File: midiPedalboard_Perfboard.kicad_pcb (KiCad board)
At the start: 8 copper layers, 66 x 50.8 mm, 49 parts, among them J1 wire, J10 wire, J11 wire, J12 wire, J13 wire, J14 wire, J15 MIDI_4, J16 MIDI_5, J17 MIDI_4, J18 MIDI_2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

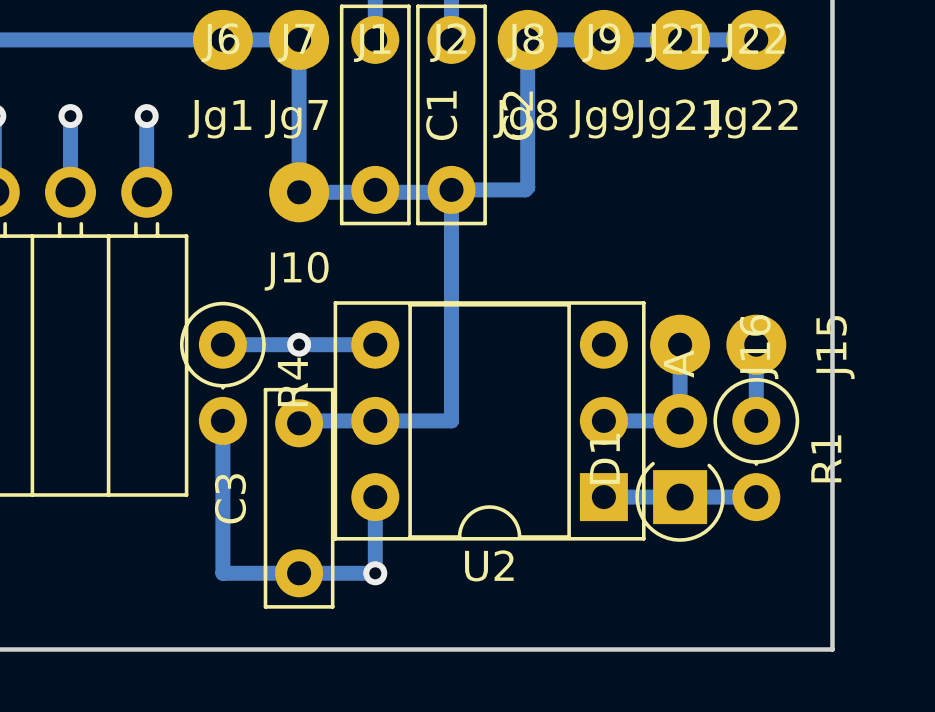
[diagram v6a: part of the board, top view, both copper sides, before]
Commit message: move pc900 part
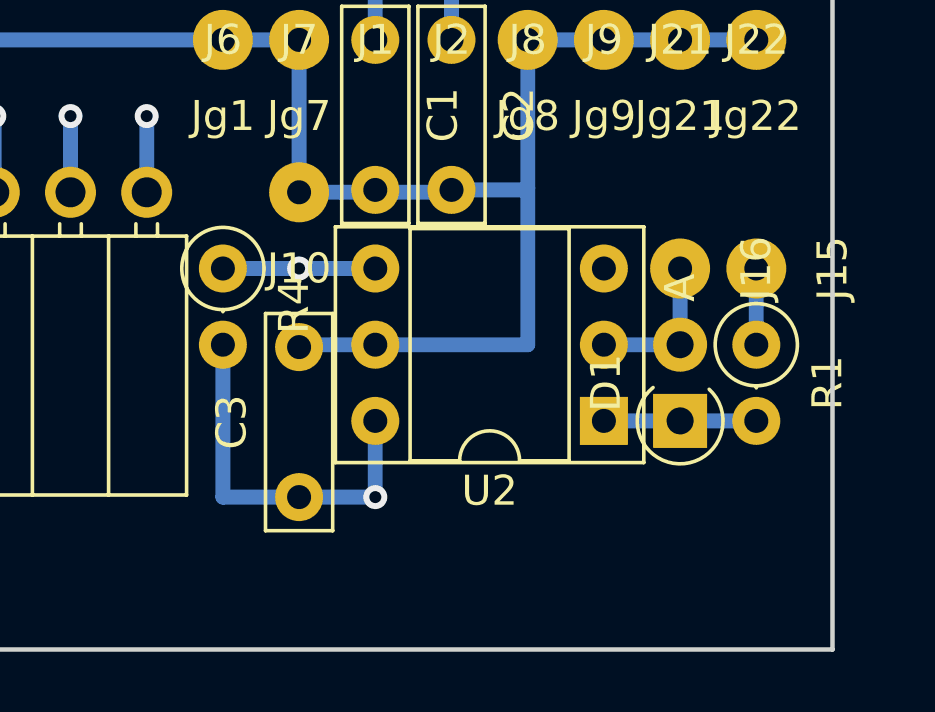
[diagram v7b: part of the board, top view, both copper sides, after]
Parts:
- moved D1 2.54 mm to (172.7, 119.4)
- moved J15 2.54 mm to (175.3, 114.3)
- moved J16 2.54 mm to (172.7, 114.3)
- moved R4 2.54 mm to (157.5, 114.3)
- moved U2 2.54 mm to (170.2, 119.4)
- moved C3 2.54 mm to (160.0, 121.9)
- moved R1 2.54 mm to (175.3, 116.8)
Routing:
- net /UART_RX: track 35.9 -> 33.3 mm
- net VCC: track 129.4 -> 126.9 mm
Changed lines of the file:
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@@
   )
   (module Diode_THT:D_A-405_P2.54mm_Vertical_AnodeUp (layer F.Cu)
-    (at 172.72 121.92 90)
+    (at 172.72 119.38 90)
     (descr "Diode, A-405 series, Axial, Vertical, pin pitch=2.54mm, , length*diameter=5.2*2.7mm^2, , http://www.diodes.com/_files/packages/A-405.pdf")
     (tags "Diode A-405 series Axial Vertical pin pitch 2.54mm  length 5.2mm diameter 2.7mm")
@@
   )
   (module Connector_Wire:SolderWirePad_1x01_Drill0.8mm (layer F.Cu)
-    (at 175.26 116.84 270)
+    (at 175.26 114.3 270)
     (descr "Wire solder connection")
     (tags connector)
@@
   )
   (module Connector_Wire:SolderWirePad_1x01_Drill0.8mm (layer F.Cu)
-    (at 172.72 116.84 270)
+    (at 172.72 114.3 270)
     (descr "Wire solder connection")
     (tags connector)
@@
   )
   (module Resistor_THT:R_Axial_DIN0207_L6.3mm_D2.5mm_P2.54mm_Vertical (layer F.Cu)
-    (at 175.26 119.38 270)
+    (at 175.26 116.84 270)
     (descr "Resistor, Axial_DIN0207 series, Axial, Vertical, pin pitch=2.54mm, 0.25W = 1/4W, length*diameter=6.3*2.5mm^2, http://cdn-reichelt.de/documents/datenblatt/B400/1_4W%23YAG.pdf")
     (tags "Resistor Axial_DIN0207 series Axial Vertical pin pitch 2.54mm 0.25W = 1/4W length 6.3mm diameter 2.5mm")
@@
   )
   (module Resistor_THT:R_Axial_DIN0207_L6.3mm_D2.5mm_P2.54mm_Vertical (layer F.Cu)
-    (at 157.48 116.84 270)
+    (at 157.48 114.3 270)
     (descr "Resistor, Axial_DIN0207 series, Axial, Vertical, pin pitch=2.54mm, 0.25W = 1/4W, length*diameter=6.3*2.5mm^2, http://cdn-reichelt.de/documents/datenblatt/B400/1_4W%23YAG.pdf")
     (tags "Resistor Axial_DIN0207 series Axial Vertical pin pitch 2.54mm 0.25W = 1/4W length 6.3mm diameter 2.5mm")
@@
   )
   (module Package_DIP:DIP-6_W7.62mm_Socket (layer F.Cu)
-    (at 170.18 121.92 180)
+    (at 170.18 119.38 180)
     (descr "6-lead though-hole mounted DIP package, row spacing 7.62 mm (300 mils), Socket")
     (tags "THT DIP DIL PDIP 2.54mm 7.62mm 300mil Socket")
@@
   )
   (module Capacitor_THT:C_Rect_L7.0mm_W2.0mm_P5.00mm (layer F.Cu)
-    (at 160.02 124.46 90)
+    (at 160.02 121.92 90)
     (descr "C, Rect series, Radial, pin pitch=5.00mm, , length*width=7*2mm^2, Capacitor")
     (tags "C Rect series Radial pin pitch 5.00mm  length 7mm width 2mm Capacitor")
@@
   (segment (start 167.56 111.68) (end 167.64 111.6) (width 0.5) (layer B.Cu) (net 2))
   (segment (start 167.64 106.68) (end 175.26 106.68) (width 0.5) (layer B.Cu) (net 2))
-  (segment (start 165.1 111.68) (end 165.1 119.38) (width 0.5) (layer B.Cu) (net 2))
-  (segment (start 160.1 119.38) (end 160.02 119.46) (width 0.5) (layer B.Cu) (net 2))
-  (segment (start 162.56 119.38) (end 160.1 119.38) (width 0.5) (layer B.Cu) (net 2))
-  (segment (start 165.1 119.38) (end 162.56 119.38) (width 0.5) (layer B.Cu) (net 2))
+  (segment (start 162.56 116.84) (end 160.1 116.84) (width 0.5) (layer B.Cu) (net 2))
   (segment (start 139.7 111.76) (end 139.7 109.22) (width 0.5) (layer B.Cu) (net 2))
   (via (at 139.7 109.22) (size 0.8) (drill 0.4) (layers F.Cu B.Cu) (net 2))
@@
   (via (at 137.16 109.22) (size 0.8) (drill 0.4) (layers F.Cu B.Cu) (net 2))
   (segment (start 135.835509 107.895509) (end 137.16 109.22) (width 0.25) (layer wire2) (net 2))
+  (segment (start 162.56 116.84) (end 167.64 116.84) (width 0.5) (layer B.Cu) (net 2))
+  (segment (start 167.64 116.84) (end 167.64 111.6) (width 0.5) (layer B.Cu) (net 2))
   (segment (start 165.1 101.6) (end 165.1 104.14) (width 0.5) (layer B.Cu) (net 3))
   (segment (start 165.1 104.14) (end 165.1 106.68) (width 0.5) (layer B.Cu) (net 3))
-  (segment (start 157.48 119.38) (end 157.48 124.46) (width 0.5) (layer B.Cu) (net 4))
-  (segment (start 157.48 124.46) (end 160.02 124.46) (width 0.5) (layer B.Cu) (net 4))
-  (segment (start 160.02 124.46) (end 162.56 124.46) (width 0.5) (layer B.Cu) (net 4))
-  (segment (start 162.56 124.46) (end 162.56 121.92) (width 0.5) (layer B.Cu) (net 4))
+  (segment (start 157.48 116.84) (end 157.48 121.92) (width 0.5) (layer B.Cu) (net 4))
+  (segment (start 157.48 121.92) (end 160.02 121.92) (width 0.5) (layer B.Cu) (net 4))
+  (segment (start 160.02 121.92) (end 162.56 121.92) (width 0.5) (layer B.Cu) (net 4))
+  (segment (start 162.56 121.92) (end 162.56 119.38) (width 0.5) (layer B.Cu) (net 4))
   (segment (start 142.24 111.76) (end 142.24 109.22) (width 0.5) (layer B.Cu) (net 4))
   (via (at 142.24 109.22) (size 0.8) (drill 0.4) (layers F.Cu B.Cu) (net 4))
@@
   (segment (start 134.62 111.76) (end 134.62 114.3) (width 0.5) (layer B.Cu) (net 4))
   (via (at 134.62 114.3) (size 0.8) (drill 0.4) (layers F.Cu B.Cu) (net 4))
-  (segment (start 158.75 120.65) (end 162.56 124.46) (width 0.25) (layer wire1) (net 4))
-  (segment (start 158.75 113.830998) (end 158.75 120.65) (width 0.25) (layer wire1) (net 4))
   (segment (start 155.409002 110.49) (end 158.75 113.830998) (width 0.25) (layer wire1) (net 4))
-  (via (at 162.56 124.46) (size 0.8) (drill 0.4) (layers F.Cu B.Cu) (net 4))
+  (via (at 162.56 121.92) (size 0.8) (drill 0.4) (layers F.Cu B.Cu) (net 4))
   (segment (start 134.62 114.3) (end 138.43 110.49) (width 0.25) (layer wire1) (net 4))
   (segment (start 138.43 110.49) (end 155.409002 110.49) (width 0.25) (layer wire1) (net 4))
   (segment (start 134.62 114.3) (end 134.62 116.84) (width 0.5) (layer B.Cu) (net 4))
-  (segment (start 170.18 121.92) (end 175.26 121.92) (width 0.5) (layer B.Cu) (net 5))
-  (segment (start 170.18 119.38) (end 172.72 119.38) (width 0.5) (layer B.Cu) (net 6))
-  (segment (start 172.72 119.38) (end 172.72 116.84) (width 0.5) (layer B.Cu) (net 6))
+  (segment (start 158.75 118.11) (end 162.56 121.92) (width 0.25) (layer wire1) (net 4))
+  (segment (start 158.75 113.830998) (end 158.75 118.11) (width 0.25) (layer wire1) (net 4))
+  (segment (start 170.18 119.38) (end 175.26 119.38) (width 0.5) (layer B.Cu) (net 5))
+  (segment (start 170.18 116.84) (end 172.72 116.84) (width 0.5) (layer B.Cu) (net 6))
+  (segment (start 172.72 116.84) (end 172.72 114.3) (width 0.5) (layer B.Cu) (net 6))
   (segment (start 154.94 101.6) (end 154.94 104.14) (width 0.5) (layer B.Cu) (net 7))
   (via (at 154.94 104.14) (size 0.8) (drill 0.4) (layers F.Cu B.Cu) (net 7))
@@
   (segment (start 165.1 86.344) (end 165.1 83.82) (width 0.5) (layer B.Cu) (net 17))
   (segment (start 167.64 86.344) (end 167.64 83.82) (width 0.5) (layer B.Cu) (net 18))
-  (segment (start 175.26 119.38) (end 175.26 116.84) (width 0.5) (layer B.Cu) (net 19))
+  (segment (start 175.26 116.84) (end 175.26 114.3) (width 0.5) (layer B.Cu) (net 19))
   (segment (start 134.62 119.38) (end 134.62 121.92) (width 0.5) (layer B.Cu) (net 20))
   (segment (start 139.7 106.68) (end 137.16 106.68) (width 0.5) (layer B.Cu) (net 21))
@@
   (segment (start 142.24 101.6) (end 142.24 104.14) (width 0.5) (layer B.Cu) (net 27))
   (via (at 142.24 104.14) (size 0.8) (drill 0.4) (layers F.Cu B.Cu) (net 27))
-  (via (at 160.02 116.84) (size 0.8) (drill 0.4) (layers F.Cu B.Cu) (net 27))
-  (segment (start 157.48 116.84) (end 160.02 116.84) (width 0.5) (layer B.Cu) (net 27))
-  (segment (start 160.02 116.84) (end 162.56 116.84) (width 0.5) (layer B.Cu) (net 27))
+  (via (at 160.02 114.3) (size 0.8) (drill 0.4) (layers F.Cu B.Cu) (net 27))
+  (segment (start 157.48 114.3) (end 160.02 114.3) (width 0.5) (layer B.Cu) (net 27))
+  (segment (start 160.02 114.3) (end 162.56 114.3) (width 0.5) (layer B.Cu) (net 27))
   (segment (start 142.24 104.14) (end 142.24 107.95) (width 0.25) (layer wire2) (net 27))
   (segment (start 142.294491 108.004491) (end 156.264491 108.004491) (width 0.25) (layer wire2) (net 27))
   (segment (start 142.24 107.95) (end 142.294491 108.004491) (width 0.25) (layer wire2) (net 27))
   (segment (start 156.264491 108.004491) (end 157.48 109.22) (width 0.25) (layer wire2) (net 27))
-  (segment (start 157.48 114.3) (end 160.02 116.84) (width 0.25) (layer wire2) (net 27))
-  (segment (start 157.48 109.22) (end 157.48 114.3) (width 0.25) (layer wire2) (net 27))
+  (segment (start 157.48 111.180248) (end 160.02 113.720248) (width 0.25) (layer wire2) (net 27))
+  (segment (start 157.48 109.22) (end 157.48 111.180248) (width 0.25) (layer wire2) (net 27))
+  (segment (start 160.02 113.720248) (end 160.02 114.3) (width 0.25) (layer wire2) (net 27))
   (segment (start 144.999918 101.953781) (end 144.999918 86.697781) (width 0.5) (layer In1.Cu) (net 30))
   (segment (start 152.619918 86.697781) (end 150.079918 86.697781) (width 0.5) (layer In1.Cu) (net 31))
